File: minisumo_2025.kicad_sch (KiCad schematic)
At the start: 90 parts, among them J1 USB_C Connector, J10 DISTANCE_R90, J11 DISTANCE_R, J12 DISTANCE_RF, J13 DISTANCE_L90, J14 DISTANCE_L, J15 LINE_LEFT, J16 DISTANCE_LF, J2 SERVO, J3 START_MODULE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

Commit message: base layout
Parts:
- removed U5: ~, footprints:SOP65P640X120-14N, symbol Logic_LevelTranslator:74AHCT125T14-13
- removed U8: TXS0108ERGYR, footprints:DQS20_TEX, symbol 2025-02-16_00-59-53:TXB0108DQSR
- added C32: 1uF, Capacitor_SMD:C_0402_1005Metric, symbol Device:C_Small
- added C33: 0.1uF, Capacitor_SMD:C_0402_1005Metric, symbol Device:C_Small
- added R7: 10k, Resistor_SMD:R_0402_1005Metric, symbol Device:R_Small
- added U5: TXS0108ERGYR, footprints:DQS20_TEX, symbol 2025-02-16_00-59-53:TXB0108DQSR
- C2: value 0.1uF -> 10uF
- J10, J11, J12, J13, J14, J15, J16, J9: footprint Connector_JST:CONN-TH_S3B-ZR-3.4-LF-SN -> footprints:CONN-TH_S3B-ZR-3.4-LF-SN
- J8: footprint Connector_JST:JST_ZH_B6B-ZR_1x06_P1.50mm_Vertical -> footprints:CONN-TH_S6B-ZR-3.4-LF-SN
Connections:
- net +3V3: now also C19.1, C27.1, C28.1, R13.1, R15.1, U6.10 (EN), U7.10 (EN), R7.1, U5.5 (VCCA)
- net +5V: now also C33.1, U5.16 (VCCB); no longer C27.1, C28.1, R13.1, R15.1, U6.10 (EN), U7.10 (EN)
- net +BATT: now also J6.2 (Pin_2); no longer C19.1, J6.1 (Pin_1)
- net D+: now also U2.1 (I/O1); no longer U2.3 (I/O2)
- net D-: now also U2.3 (I/O2); no longer U2.1 (I/O1)
- net DISTANCE_L: now also U5.8 (A6)
- net DISTANCE_L90: now also U5.9 (A7)
- net DISTANCE_L90_OUT: now also U5.12 (B7)
- net DISTANCE_LF: now also U5.7 (A5)
- net DISTANCE_LF_OUT: now also U5.14 (B5)
- net DISTANCE_L_OUT: now also U5.13 (B6)
- net DISTANCE_R: now also U5.2 (A2)
- net DISTANCE_R90: now also U5.1 (A1)
- net DISTANCE_R90_OUT: now also U5.20 (B1)
- net DISTANCE_RF: now also U5.3 (A3)
- net DISTANCE_RF_OUT: now also U5.18 (B3)
- net DISTANCE_R_OUT: now also U5.19 (B2)
- net D_N: now also U2.4 (I/O2); no longer U2.6 (I/O1)
- net D_P: now also U2.6 (I/O1); no longer U2.4 (I/O2)
- net ESP_BOOT: now also R7.2
- net ESP_EN: now also C32.2
- net GND: now also J6.1 (Pin_1), C32.1, C33.2, U5.17 (B4), U5.4 (A4); no longer J6.2 (Pin_2)
- net GPIO17: now reaches U3.10 (IO17)
- net GPIO18: now reaches U3.11 (IO18)
- net GPIO8: now reaches U3.12 (IO8)
- net GPIO9: now reaches U3.17 (IO9)
- net GPIO10: now reaches U3.18 (IO10)
- net GPIO11: now reaches U3.19 (IO11)
- net GPIO12: now reaches U3.20 (IO12)
- net GPIO13: now reaches U3.21 (IO13)
- net GPIO14: now reaches U3.22 (IO14)
- net GPIO21: now reaches U3.23 (IO21)
- net GPIO47: now reaches U3.24 (IO47)
- net GPIO48: now reaches U3.25 (IO48)
- net GPIO35: now reaches U3.28 (IO35)
- net GPIO36: now reaches U3.29 (IO36)
- net GPIO37: now reaches U3.30 (IO37)
- net GPIO38: now reaches U3.31 (IO38)
- net GPIO2: now reaches U3.38 (IO2)
- net GPIO1: now reaches U3.39 (IO1)
- net GPIO4: now reaches U3.4 (IO4)
- net GPIO5: now reaches U3.5 (IO5)
- net GPIO6: now reaches U3.6 (IO6)
- net GPIO7: now reaches U3.7 (IO7)
- net GPIO15: now reaches U3.8 (IO15)
- net GPIO16: now reaches U3.9 (IO16)
- no-connect marks 22 -> 28
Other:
- note added: "Pinout"
- note added: "TODO: - is the level shifting good - add jumpers to choose to use or not to use the logic converter - how should i route the different grounds for regulator and drivers?"
- note removed: "TODO: - is there protection needed for vbus and 5v line? - is the level shifting good? - how should i route the different grounds for regulator and drivers? - bigger capacitors on the drivers? - change voltage divider for switcing"
- moved on the sheet: C12, C18, J10, J11, J12, J13, J14, J16, J8, R1, SW5A, U2

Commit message: changes
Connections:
- net IN1_1 is gone; now on net GPIO38: U6.2 (IN1)
- net IN1_2 is gone; now on net GPIO2: U7.2 (IN1)
- net IN2_1 is gone; now on net GPIO37: U6.1 (IN2)
- net IN2_2 is gone; now on net GPIO1: U7.1 (IN2)
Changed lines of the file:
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@@
+		)
+	)
+	(label "IN1_2"
+		(at 327.66 54.61 0)
+		(effects
+			(font
+				(size 1.27 1.27)
+			)
+			(justify left bottom)
 		)
 	)
@@
 		)
 	)
+	(label "IN1_1"
+		(at 360.68 74.93 0)
+		(effects
+			(font
+				(size 1.27 1.27)
+			)
+			(justify left bottom)
+		)
+	)
 	(label "GPIO6"
 		(at 55.88 54.61 180)
@@
 		)
 	)
+	(label "IN2_1"
+		(at 360.68 72.39 0)
+		(effects
+			(font
+				(size 1.27 1.27)
+			)
+			(justify left bottom)
+		)
+	)
 	(label "GPIO1"
 		(at 322.58 52.07 180)
@@
 		(effects
 			(font
+				(size 1.27 1.27)
+			)
+			(justify left bottom)
+		)
+	)
+	(label "IN2_2"
+		(at 327.66 52.07 0)
+		(effects
+			(font

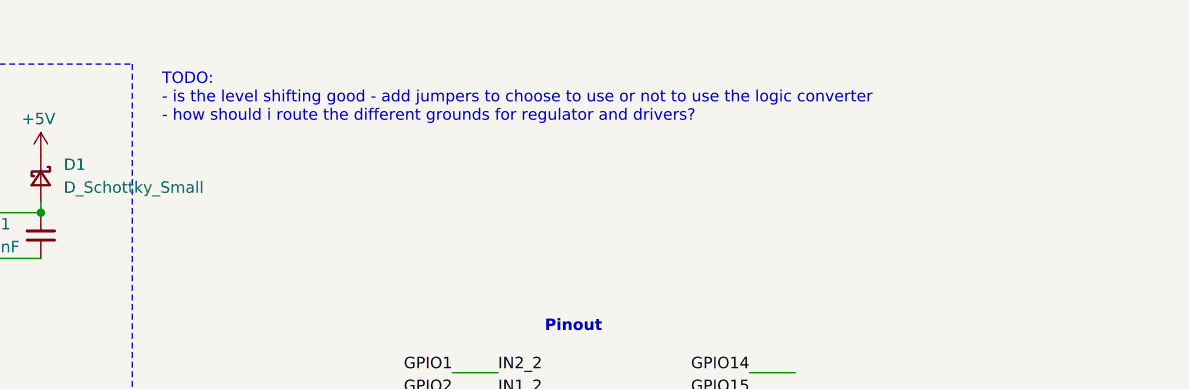
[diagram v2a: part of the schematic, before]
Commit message: more driver traces
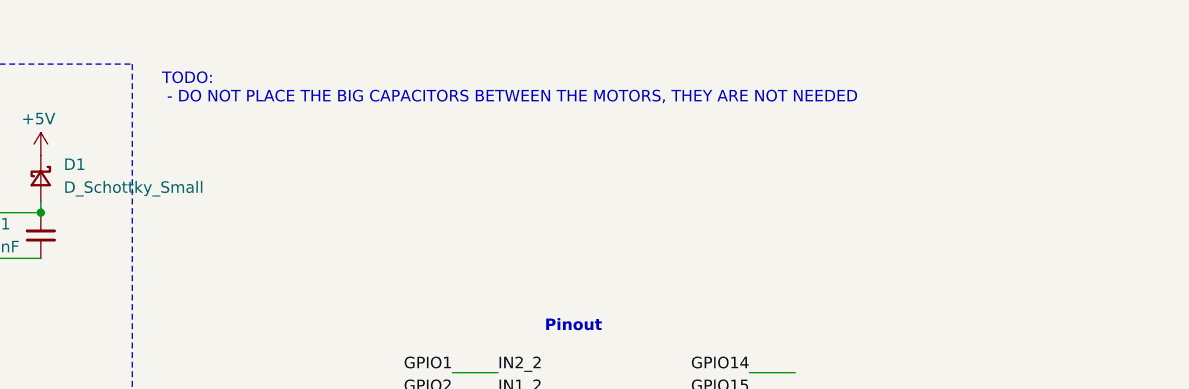
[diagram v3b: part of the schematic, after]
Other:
- note added: "TODO: - DO NOT PLACE THE BIG CAPACITORS BETWEEN THE MOTORS, THEY ARE NOT NEEDED"
- note removed: "TODO: - is the level shifting good - add jumpers to choose to use or not to use the logic converter - how should i route the different grounds for regulator and drivers?"
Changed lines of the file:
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@@
 		)
 	)
-	(text "TODO:\n- is the level shifting good - add jumpers to choose to use or not to use the logic converter\n- how should i route the different grounds for regulator and drivers?\n\n"
+	(text "TODO:\n - DO NOT PLACE THE BIG CAPACITORS BETWEEN THE MOTORS, THEY ARE NOT NEEDED\n\n\n"
 		(exclude_from_sim no)
 		(at 290.322 22.606 0)

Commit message: more routing
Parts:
- removed C30, C31: 470uF, Capacitor_THT:C_Radial_D10.0mm_H16.0mm_P5.00mm, symbol Device:C_Small
- J6: footprint Connector_Wire:SolderWire-0.5sqmm_1x02_P4.8mm_D0.9mm_OD2.3mm -> Connector_AMASS:AMASS_XT30U-F_1x02_P5.0mm_Vertical
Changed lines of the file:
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@@
 	)
 	(junction
-		(at 91.44 144.78)
-		(diameter 0)
-		(color 0 0 0 0)
-	)
-	(junction
 		(at 76.2 22.86)
 		(diameter 0)
@@
 	)
 	(junction
-		(at 231.14 151.13)
-		(diameter 0)
-		(color 0 0 0 0)
-	)
-	(junction
 		(at 276.86 34.29)
 		(diameter 0)
@@
 	)
 	(junction
-		(at 231.14 146.05)
-		(diameter 0)
-		(color 0 0 0 0)
-	)
-	(junction
-		(at 91.44 149.86)
-		(diameter 0)
-		(color 0 0 0 0)
-	)
-	(junction
 		(at 20.32 81.28)
 		(diameter 0)
@@
 	(wire
 		(pts
-			(xy 231.14 146.05) (xy 240.03 146.05)
-		)
-		(stroke
-			(width 0)
-			(type default)
-		)
-	)
-	(wire
-		(pts
 			(xy 171.45 156.21) (xy 181.61 156.21)
 		)
@@
 	(wire
 		(pts
-			(xy 73.66 149.86) (xy 91.44 149.86)
-		)
-		(stroke
-			(width 0)
-			(type default)
-		)
-	)
-	(wire
-		(pts
 			(xy 222.25 74.93) (xy 222.25 67.31)
 		)
@@
 	(wire
 		(pts
-			(xy 231.14 151.13) (xy 240.03 151.13)
+			(xy 212.09 151.13) (xy 240.03 151.13)
 		)
 		(stroke
@@
 	(wire
 		(pts
-			(xy 101.6 144.78) (xy 91.44 144.78)
+			(xy 83.82 144.78) (xy 101.6 144.78)
 		)
 		(stroke
@@
 	(wire
 		(pts
-			(xy 91.44 149.86) (xy 101.6 149.86)
+			(xy 73.66 149.86) (xy 101.6 149.86)
 		)
 		(stroke
@@
 	(wire
 		(pts
-			(xy 222.25 146.05) (xy 231.14 146.05)
+			(xy 222.25 146.05) (xy 240.03 146.05)
 		)
 		(stroke
@@
 	(wire
 		(pts
-			(xy 212.09 151.13) (xy 231.14 151.13)
-		)
-		(stroke
-			(width 0)
-			(type default)
-		)
-	)
-	(wire
-		(pts
 			(xy 77.47 154.94) (xy 73.66 154.94)
 		)
@@
 	(wire
 		(pts
-			(xy 91.44 144.78) (xy 83.82 144.78)
-		)
-		(stroke
-			(width 0)
-			(type default)
-		)
-	)
-	(wire
-		(pts
 			(xy 30.48 118.11) (xy 33.02 118.11)
 		)
@@
 	)
 	(symbol
-		(lib_id "Device:C_Small")
-		(at 231.14 148.59 0)
-		(mirror y)
-		(unit 1)
-		(exclude_from_sim no)
-		(in_bom yes)
-		(on_board yes)
-		(dnp no)
-		(property "Reference" "C31"
-			(at 236.982 147.32 0)
-			(effects
-				(font
-					(size 1.27 1.27)
-				)
-				(justify left)
-			)
-		)
-		(property "Value" "470uF"
-			(at 238.252 149.352 0)
-			(effects
-				(font
-					(size 1.27 1.27)
-				)
-				(justify left)
-			)
-		)
-		(property "Footprint" "Capacitor_THT:C_Radial_D10.0mm_H16.0mm_P5.00mm"
-			(at 231.14 148.59 0)
-			(effects
-				(font
-					(size 1.27 1.27)
-				)
-				(hide yes)
-			)
-		)
-		(property "Datasheet" "~"
-			(at 231.14 148.59 0)
-			(effects
-				(font
-					(size 1.27 1.27)
-				)
-				(hide yes)
-			)
-		)
-		(property "Description" "Unpolarized capacitor, small symbol"
-			(at 231.14 148.59 0)
-			(effects
-				(font
-					(size 1.27 1.27)
-				)
-				(hide yes)
-			)
-		)
-		(pin "1"
-		)
-		(pin "2"
-		)
-		(instances
-			(project "minisumo_2025"
-				(path "/cdca51c8-556b-4873-bdb8-43b7170e2006"
-					(reference "C31")
-					(unit 1)
-				)
-			)
-		)
-	)
-	(symbol
 		(lib_id "Connector:Conn_01x03_Socket")
 		(at 33.02 261.62 0)
@@
 	)
 	(symbol
-		(lib_id "Device:C_Small")
-		(at 91.44 147.32 0)
-		(mirror y)
-		(unit 1)
-		(exclude_from_sim no)
-		(in_bom yes)
-		(on_board yes)
-		(dnp no)
-		(property "Reference" "C30"
-			(at 97.282 146.05 0)
-			(effects
-				(font
-					(size 1.27 1.27)
-				)
-				(justify left)
-			)
-		)
-		(property "Value" "470uF"
-			(at 98.552 148.082 0)
-			(effects
-				(font
-					(size 1.27 1.27)
-				)
-				(justify left)
-			)
-		)
-		(property "Footprint" "Capacitor_THT:C_Radial_D10.0mm_H16.0mm_P5.00mm"
-			(at 91.44 147.32 0)
-			(effects
-				(font
-					(size 1.27 1.27)
-				)
-				(hide yes)
-			)
-		)
-		(property "Datasheet" "~"
-			(at 91.44 147.32 0)
-			(effects
-				(font
-					(size 1.27 1.27)
-				)
-				(hide yes)
-			)
-		)
-		(property "Description" "Unpolarized capacitor, small symbol"
-			(at 91.44 147.32 0)
-			(effects
-				(font
-					(size 1.27 1.27)
-				)
-				(hide yes)
-			)
-		)
-		(pin "1"
-		)
-		(pin "2"
-		)
-		(instances
-			(project "minisumo_2025"
-				(path "/cdca51c8-556b-4873-bdb8-43b7170e2006"
-					(reference "C30")
-					(unit 1)
-				)
-			)
-		)
-	)
-	(symbol
 		(lib_id "power:+5V")
 		(at 19.05 132.08 0)
@@
 		(on_board yes)
 		(dnp no)
-		(fields_autoplaced yes)
 		(property "Reference" "J6"
 			(at 165.1 76.1999 0)
@@
 			)
 		)
-		(property "Footprint" "Connector_Wire:SolderWire-0.5sqmm_1x02_P4.8mm_D0.9mm_OD2.3mm"
+		(property "Footprint" "Connector_AMASS:AMASS_XT30U-F_1x02_P5.0mm_Vertical"
 			(at 166.37 76.2 0)
 			(effects

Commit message: driver routing
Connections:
- net +3V3: no longer C19.1
- net +BATT: now also C19.1
- net GPIO1: no longer U7.1 (IN2)
- net GPIO2: no longer U7.2 (IN1)
- net GPIO35: now also U7.1 (IN2)
- net GPIO36: now also U7.2 (IN1)
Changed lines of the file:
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@@
 		)
 	)
+	(label "IN2_2"
+		(at 360.68 67.31 0)
+		(effects
+			(font
+				(size 1.27 1.27)
+			)
+			(justify left bottom)
+		)
+	)
 	(label "MOTOR2_A"
 		(at 222.25 148.59 180)
@@
 		)
 	)
-	(label "START"
-		(at 120.65 92.71 0)
+	(label "IN1_1"
+		(at 360.68 74.93 0)
 		(effects
 			(font
@@
 		)
 	)
-	(label "SERVO_PWM"
-		(at 228.6 195.58 0)
+	(label "START"
+		(at 120.65 92.71 0)
 		(effects
 			(font
@@
 		)
 	)
-	(label "IN1_2"
-		(at 327.66 54.61 0)
+	(label "SERVO_PWM"
+		(at 228.6 195.58 0)
 		(effects
 			(font
@@
 		)
 	)
+	(label "IN2_1"
+		(at 360.68 72.39 0)
+		(effects
+			(font
+				(size 1.27 1.27)
+			)
+			(justify left bottom)
+		)
+	)
 	(label "LINE_RIGHT"
 		(at 140.97 209.55 180)
@@
 		)
 	)
-	(label "IN1_1"
-		(at 360.68 74.93 0)
-		(effects
-			(font
-				(size 1.27 1.27)
-			)
-			(justify left bottom)
-		)
-	)
 	(label "GPIO6"
 		(at 55.88 54.61 180)
@@
 		)
 	)
-	(label "IN2_2"
-		(at 163.83 203.2 0)
-		(effects
-			(font
-				(size 1.27 1.27)
-			)
-			(justify left bottom)
-		)
-	)
 	(label "START"
 		(at 228.6 198.12 0)
@@
 		)
 	)
-	(label "IN1_1"
-		(at 163.83 195.58 0)
-		(effects
-			(font
-				(size 1.27 1.27)
-			)
-			(justify left bottom)
-		)
-	)
 	(label "GPIO17"
 		(at 355.6 59.69 180)
@@
 		)
 	)
-	(label "IN1_2"
-		(at 163.83 200.66 0)
-		(effects
-			(font
-				(size 1.27 1.27)
-			)
-			(justify left bottom)
-		)
-	)
 	(label "GPIO11"
 		(at 322.58 74.93 180)
@@
 		)
 	)
+	(label "IN1_2"
+		(at 360.68 69.85 0)
+		(effects
+			(font
+				(size 1.27 1.27)
+			)
+			(justify left bottom)
+		)
+	)
 	(label "ND2_1"
 		(at 24.13 168.91 270)
@@
 		)
 	)
-	(label "IN2_1"
-		(at 360.68 72.39 0)
-		(effects
-			(font
-				(size 1.27 1.27)
-			)
-			(justify left bottom)
-		)
-	)
 	(label "GPIO1"
 		(at 322.58 52.07 180)
@@
 		)
 	)
-	(label "IN2_1"
-		(at 163.83 198.12 0)
-		(effects
-			(font
-				(size 1.27 1.27)
-			)
-			(justify left bottom)
-		)
-	)
 	(label "DISTANCE_RF"
 		(at 195.58 200.66 0)
@@
 		)
 	)
-	(label "IN2_2"
-		(at 327.66 52.07 0)
-		(effects
-			(font
-				(size 1.27 1.27)
-			)
-			(justify left bottom)
-		)
-	)
 	(symbol
 		(lib_id "Device:LED_Small")
@@
 	)
 	(symbol
-		(lib_id "power:+3V3")
-		(at 48.26 121.92 0)
-		(unit 1)
-		(exclude_from_sim no)
-		(in_bom yes)
-		(on_board yes)
-		(dnp no)
-		(property "Reference" "#PWR036"
-			(at 48.26 125.73 0)
-			(effects
-				(font
-					(size 1.27 1.27)
-				)
-				(hide yes)
-			)
-		)
-		(property "Value" "+3V3"
-			(at 48.26 118.364 0)
-			(effects
-				(font
-					(size 1.27 1.27)
-				)
-			)
-		)
-		(property "Footprint" ""
-			(at 48.26 121.92 0)
-			(effects
-				(font
-					(size 1.27 1.27)
-				)
-				(hide yes)
-			)
-		)
-		(property "Datasheet" ""
-			(at 48.26 121.92 0)
-			(effects
-				(font
-					(size 1.27 1.27)
-				)
-				(hide yes)
-			)
-		)
-		(property "Description" "Power symbol creates a global label with name \"+3V3\""
-			(at 48.26 121.92 0)
-			(effects
-				(font
-					(size 1.27 1.27)
-				)
-				(hide yes)
-			)
-		)
-		(pin "1"
-		)
-		(instances
-			(project "minisumo_2025"
-				(path "/cdca51c8-556b-4873-bdb8-43b7170e2006"
-					(reference "#PWR036")
-					(unit 1)
-				)
-			)
-		)
-	)
-	(symbol
 		(lib_id "Switch:SW_Push_Dual_x2")
 		(at 25.4 77.47 0)
@@
 	)
 	(symbol
+		(lib_id "power:+BATT")
+		(at 48.26 121.92 0)
+		(unit 1)
+		(exclude_from_sim no)
+		(in_bom yes)
+		(on_board yes)
+		(dnp no)
+		(fields_autoplaced yes)
+		(property "Reference" "#PWR036"
+			(at 48.26 125.73 0)
+			(effects
+				(font
+					(size 1.27 1.27)
+				)
+				(hide yes)
+			)
+		)
+		(property "Value" "+BATT"
+			(at 48.26 116.84 0)
+			(effects
+				(font
+					(size 1.27 1.27)
+				)
+			)
+		)
+		(property "Footprint" ""
+			(at 48.26 121.92 0)
+			(effects
+				(font
+					(size 1.27 1.27)
+				)
+				(hide yes)
+			)
+		)
+		(property "Datasheet" ""
+			(at 48.26 121.92 0)
+			(effects
+				(font
+					(size 1.27 1.27)
+				)
+				(hide yes)
+			)
+		)
+		(property "Description" "Power symbol creates a global label with name \"+BATT\""
+			(at 48.26 121.92 0)
+			(effects
+				(font
+					(size 1.27 1.27)
+				)
+				(hide yes)
+			)
+		)
+		(pin "1"
+		)
+		(instances
+			(project "minisumo_2025"
+				(path "/cdca51c8-556b-4873-bdb8-43b7170e2006"
+					(reference "#PWR036")
+					(unit 1)
+				)
+			)
+		)
+	)
+	(symbol
 		(lib_id "power:GND")
 		(at 116.84 34.29 0)
@@
 	)
 	(symbol
+		(lib_id "power:+BATT")
+		(at 186.69 123.19 0)
+		(unit 1)
+		(exclude_from_sim no)
+		(in_bom yes)
+		(on_board yes)
+		(dnp no)
+		(fields_autoplaced yes)
+		(property "Reference" "#PWR041"
+			(at 186.69 127 0)
+			(effects
+				(font
+					(size 1.27 1.27)
+				)
+				(hide yes)
+			)
+		)
+		(property "Value" "+BATT"
+			(at 186.69 118.11 0)
+			(effects
+				(font
+					(size 1.27 1.27)
+				)
+			)
+		)
+		(property "Footprint" ""
+			(at 186.69 123.19 0)
+			(effects
+				(font
+					(size 1.27 1.27)
+				)
+				(hide yes)
+			)
+		)
+		(property "Datasheet" ""
+			(at 186.69 123.19 0)
+			(effects
+				(font
+					(size 1.27 1.27)
+				)
+				(hide yes)
+			)
+		)
+		(property "Description" "Power symbol creates a global label with name \"+BATT\""
+			(at 186.69 123.19 0)
+			(effects
+				(font
+					(size 1.27 1.27)
+				)
+				(hide yes)
+			)
+		)
+		(pin "1"
+		)
+		(instances
+			(project "minisumo_2025"
+				(path "/cdca51c8-556b-4873-bdb8-43b7170e2006"
+					(reference "#PWR041")
+					(unit 1)
+				)
+			)
+		)
+	)
+	(symbol
 		(lib_id "power:GND")
 		(at 133.35 83.82 0)
@@
 					(unit 1)
 				)
-			)
-		)
-	)
-	(symbol
-		(lib_id "power:+BATT")
-		(at 186.69 123.19 0)
-		(unit 1)
-		(exclude_from_sim no)
-		(in_bom yes)
-		(on_board yes)
-		(dnp no)
-		(fields_autoplaced yes)
-		(property "Reference" "#PWR041"
-			(at 186.69 127 0)
-			(effects
-				(font
-					(size 1.27 1.27)
-				)
-				(hide yes)
-			)
-		)
-		(property "Value" "+BATT"
-			(at 186.69 118.11 0)
-			(effects
-				(font
-					(size 1.27 1.27)
-				)
-			)
-		)
-		(property "Footprint" ""
-			(at 186.69 123.19 0)
-			(effects
-				(font
-					(size 1.27 1.27)
-				)
-				(hide yes)
-			)
-		)
-		(property "Datasheet" ""
-			(at 186.69 123.19 0)
-			(effects
-				(font
-					(size 1.27 1.27)
-				)
-				(hide yes)
-			)
-		)
-		(property "Description" "Power symbol creates a global label with name \"+BATT\""
-			(at 186.69 123.19 0)
-			(effects
-				(font
-					(size 1.27 1.27)
-				)
-				(hide yes)
-			)
-		)
-		(pin "1"
-		)
-		(instances
-			(project "minisumo_2025"
-				(path "/cdca51c8-556b-4873-bdb8-43b7170e2006"
-					(reference "#PWR041")
-					(unit 1)
-				)

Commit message: routing
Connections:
- net GPIO35: now also U6.1 (IN2); no longer U7.1 (IN2)
- net GPIO36: now also U6.2 (IN1); no longer U7.2 (IN1)
- net GPIO37: now also U7.1 (IN2); no longer U6.1 (IN2)
- net GPIO38: now also U7.2 (IN1); no longer U6.2 (IN1)
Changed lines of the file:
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@@
+		)
+	)
+	(label "IN2_2"
+		(at 360.68 72.39 0)
+		(effects
+			(font
+				(size 1.27 1.27)
+			)
+			(justify left bottom)
 		)
 	)
@@
 		)
 	)
-	(label "IN2_2"
-		(at 360.68 67.31 0)
-		(effects
-			(font
-				(size 1.27 1.27)
-			)
-			(justify left bottom)
-		)
-	)
 	(label "MOTOR2_A"
 		(at 222.25 148.59 180)
@@
 		)
 	)
+	(label "IN2_1"
+		(at 360.68 67.31 0)
+		(effects
+			(font
+				(size 1.27 1.27)
+			)
+			(justify left bottom)
+		)
+	)
 	(label "DISTANCE_R"
 		(at 195.58 198.12 0)
@@
 		)
 	)
-	(label "IN1_1"
+	(label "IN1_2"
 		(at 360.68 74.93 0)
 		(effects
@@
 		)
 	)
-	(label "IN2_1"
-		(at 360.68 72.39 0)
-		(effects
-			(font
-				(size 1.27 1.27)
-			)
-			(justify left bottom)
-		)
-	)
 	(label "LINE_RIGHT"
 		(at 140.97 209.55 180)
@@
 	)
 	(label "IN1_1"
+		(at 360.68 69.85 0)
+		(effects
+			(font
+				(size 1.27 1.27)
+			)
+			(justify left bottom)
+		)
+	)
+	(label "IN1_1"
 		(at 34.29 147.32 0)
 		(effects
@@
 		)
 	)
-	(label "IN1_2"
-		(at 360.68 69.85 0)
-		(effects
-			(font
-				(size 1.27 1.27)
-			)
-			(justify left bottom)
-		)
-	)
